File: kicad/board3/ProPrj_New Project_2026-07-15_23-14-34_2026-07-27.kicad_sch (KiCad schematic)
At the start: 143 parts, among them P1 WJ500V-5.08-2P, P2 WJ500V-5.08-2P, Q1 AO4406A, Q2 AO4406A, SW1 HX TS4538CJ 250gf 009, SW2 HX TS4538CJ 250gf 009, SW3 HX TS4538CJ 250gf 009, SW4 HX TS4538CJ 250gf 009, SW6 HX TS4538CJ 250gf 009, SW7 HX TS4538CJ 250gf 009, U1 STM32H755ZIT6, U11 AW9523BTQR, U12 AW9523BTQR, U2 W25Q256JVEIQ, U3 TPS563201DDCR, U4 CH224K, U5 LM74700QDBVRQ1, U6 LM74700QDBVRQ1, U7 FM24CL64B-GTR, U8 TJA1051T/3/1J, U9 TJA1051T/3/1J, X1 25MHz

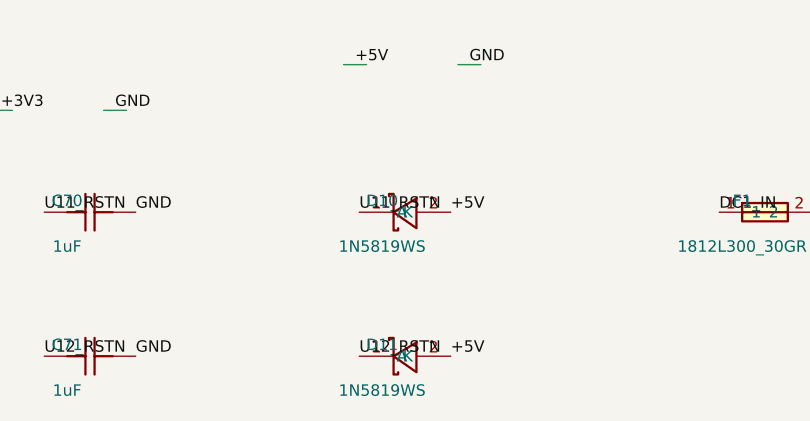
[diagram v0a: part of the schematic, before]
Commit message: fix(kicad): U31 -- reverse D10/D11, the CRITICAL that five of six lenses found
Both Schottkys were installed backwards: cathode on RSTN, anode on +5V, the
opposite of what their own commit message specified. The diode forward-biased
during the rail ramp, so C70/C71 charged through it rather than through R60/R61
and RSTN crossed its fixed 1.4 V VIH at VCC around 1.5-1.6 V -- BELOW VPOR
(1.8 V typ). Reset assertion duration was exactly zero at every ramp rate, and
the brownout half failed in the same direction. Worse than fitting no diode,
which would at least have delivered ~335 us of power-up hold. The 2026-07-31
CRITICAL was never actually closed.

Fixed on both sides with ZERO copper movement.

Schematic: D10/D11 are connected by labels sitting at fixed pin coordinates, not
by drawn wires, so rotating each symbol 180 degrees swaps which pin lands under
which label. The symbol is pin-symmetric (+/-5.08 mm, y=0), so the rotation is
exact.

Board: pads are mirror-exact about the footprint origin -- measured 0 nm error,
+/-1.172 mm, identical sizes -- so a 180 degree rotation puts pad 1 precisely
where pad 2 was. Rotate, then swap the pad nets to match, and every existing
track endpoint still lands on a pad of the correct net. D10 pad 1 now sits at
(95.992, 92.260), exactly where pad 2 was, on the +5V copper.

Doing one half alone is a trap either way: rotating without swapping nets shorts
RSTN to +5V, because pad NUMBERS carry the nets; swapping nets without rotating
leaves the silk cathode band on the wrong end.

VERIFIED BY PIN FUNCTION, not pin number -- KTD27, which is the lesson this
defect taught. The exported netlist now reads:

    /+5V       <- D10 pin 1 func=K_1,  D11 pin 1 func=K_1
    /U11_RSTN  <- D10 pin 2 func=A_2
    /U12_RSTN  <- D11 pin 2 func=A_2

The gate that let this through asserted /U11_RSTN carries IC.23 + R.2 + C.1 +
D.1. Pin 1 IS the cathode, so it passed while the circuit was inverted.

One consequence handled: the rotation carried D10/D11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
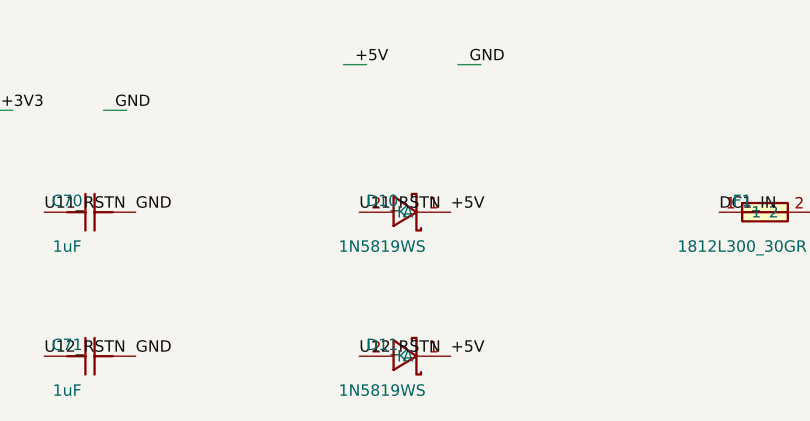
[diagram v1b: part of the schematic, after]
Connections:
- net +5V: now also D10.1 (K), D11.1 (K); no longer D10.2 (A), D11.2 (A)
- net U11_RSTN: now also D10.2 (A); no longer D10.1 (K)
- net U12_RSTN: now also D11.2 (A); no longer D11.1 (K)
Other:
- moved on the sheet: D10, D11
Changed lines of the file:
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@@
 	(symbol
 		(lib_id "JLCImport:1N5819WS")
-		(at 130.0 372.0 0)
+		(at 130.0 372.0 180)
 		(unit 1)
 		(exclude_from_sim no)
@@
 	(symbol
 		(lib_id "JLCImport:1N5819WS")
-		(at 130.0 388.0 0)
+		(at 130.0 388.0 180)
 		(unit 1)
 		(exclude_from_sim no)

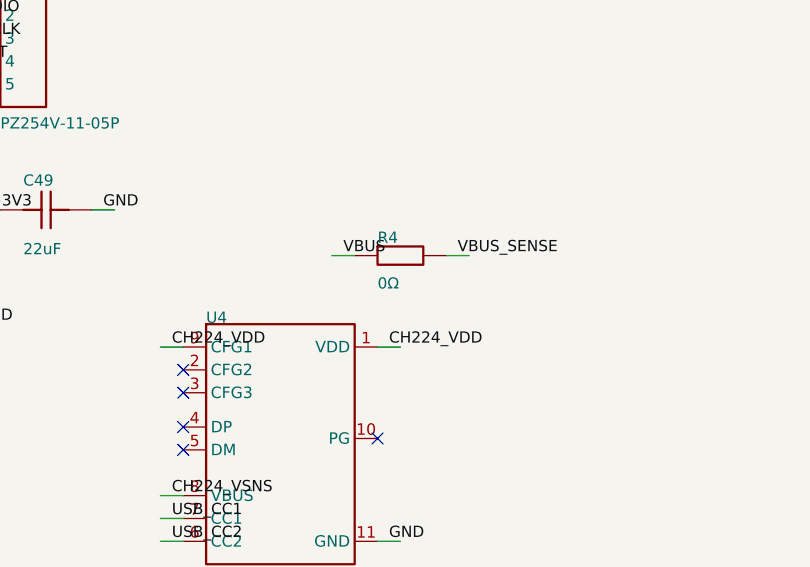
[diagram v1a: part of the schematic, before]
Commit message: fix(kicad): U48 -- R4 0 ohm to 10k, closing the PA9 injection path with no copper
R4 sat at 0 ohm between /VBUS and /VBUS_SENSE, which is a single net reaching
exactly two pads: R4.2 and U1.98 (PA9). PA9 is 5 V tolerant, but ST's tolerance
is conditional on VDD being PRESENT -- and 3.3 V here is DERIVED from 5 V through
U3. So during the buck's soft-start there is a window where 5 V sits on PA9
through 0 ohm while VDD is still rising, and current into the ESD clamp is
limited only by the clamp itself (~10-50 ohm): tens of mA against a documented
+/-5 mA pin injection limit, on EVERY power-up.

The plan called for a 100k/100k divider, which means a new part placed and
routed. 10 kOhm alone does better for zero board change:

  injection during VDD ramp   unlimited  ->  (5 - Vclamp)/10k = ~110 uA
  PA9 with USB absent         floats     ->  pulled low by PA9's internal ~40k
  PA9 with USB present        --         ->  5 x 40/50 = 4.0 V, VIH is 2.31 V

Worst-case internal pull-down across its 30-50k spread gives 3.75-4.17 V, so the
high level holds either way, and the low level no longer depends on nothing.

FIRMWARE DEPENDENCY, and it is load-bearing: PA9 must be configured with its
internal pull-down enabled (GPIOx_PUPDR). Without it the pin still floats when
USB is unplugged and VBUS sensing reads indeterminate -- the hardware half of
this fix is the current limit, the firmware half is the defined low. Nothing
configures PA9 today.

Free consequence: R4 was the board's ONLY 0 ohm part, and 10k on R0603 is
already fitted 12 times. It merges into that line, so the BOM drops 46 -> 45 and
an entire part number leaves the order. Same footprint, so no board edit and no
sync -- the U10/U24 precedent.

DRC unchanged, BOM/CPL symmetric at 143, kicad_lcsc.py check PASS.

Co-Authored-By: Claude Opus 5 (1M context) <noreply@anthropic.com>
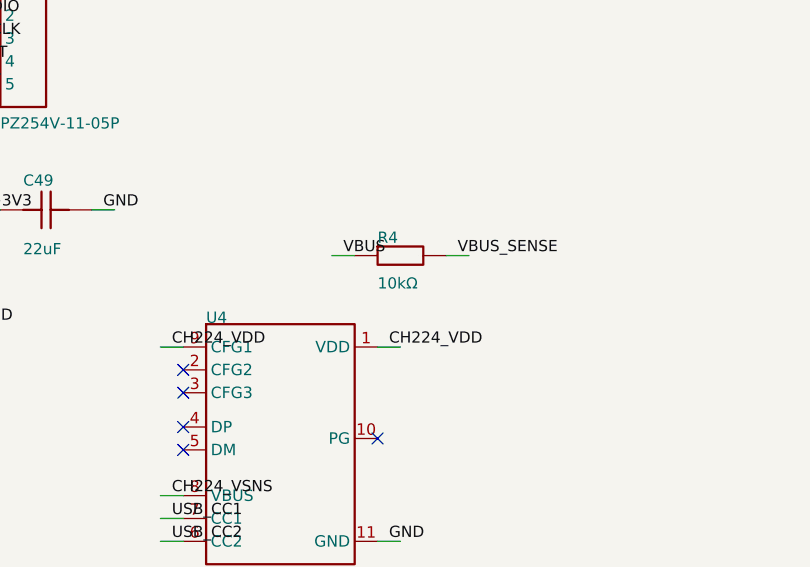
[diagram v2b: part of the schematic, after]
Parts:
- R4: value 0Ω -> 10kΩ; symbol ProPrj_New-easyedapro:0603WAF0000T5E -> ProPrj_New-easyedapro:0603WAF1002T5E; LCSC Part Name 0Ω ±1% 100mW 厚膜电阻 -> 厚膜电阻 10kΩ ±1% 100mW; Manufacturer Part 0603WAF0000T5E -> 0603WAF1002T5E; Supplier Part C21189 -> C25804
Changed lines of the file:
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@@
 	)
 	(symbol
-		(lib_id "ProPrj_New-easyedapro:0603WAF0000T5E")
+		(lib_id "ProPrj_New-easyedapro:0603WAF1002T5E")
 		(at 358.14 59.69 0)
 		(unit 1)
@@
 			)
 		)
-		(property "Value" "0Ω"
+		(property "Value" "10kΩ"
 			(at 355.6 63.5 0)
 			(show_name no)
@@
 			)
 		)
-		(property "Datasheet" "https://item.szlcsc.com/datasheet/0603WAF0000T5E/21903.html"
+		(property "Datasheet" "https://item.szlcsc.com/datasheet/0603WAF1002T5E/26547.html"
 			(at 358.14 59.69 0)
 			(hide yes)
@@
 			)
 		)
-		(property "Description" "Type:Thick Film Resistor Resistance:0Ω Tolerance:±1% Tolerance:±1% Power(Watts):100mW Voltage-Supply(Max):75V Temperature Coefficient:- Temperature Coefficient:- Operating Temperature:-55℃~+155℃ Operating Temperature:-55℃~+155℃"
+		(property "Description" "Type:Thick Film Resistor Resistance:10kΩ Tolerance:±1% Tolerance:±1% Power(Watts):100mW Voltage-Supply(Max):75V Temperature Coefficient:±100ppm/℃ Temperature Coefficient:±100ppm/℃ Operating Temperature:-55℃~+155℃ Operating Temperature:-55℃~+155℃"
 			(at 358.14 59.69 0)
 			(hide yes)
@@
 			)
 		)
-		(property "Manufacturer Part" "0603WAF0000T5E"
+		(property "Manufacturer Part" "0603WAF1002T5E"
 			(at 358.14 59.69 0)
 			(hide yes)
@@
 			)
 		)
-		(property "Supplier Part" "C21189"
+		(property "Supplier Part" "C25804"
 			(at 358.14 59.69 0)
 			(hide yes)
@@
 			)
 		)
-		(property "LCSC Part Name" "0Ω ±1% 100mW 厚膜电阻"
+		(property "LCSC Part Name" "厚膜电阻 10kΩ ±1% 100mW"
 			(at 358.14 59.69 0)
 			(hide yes)

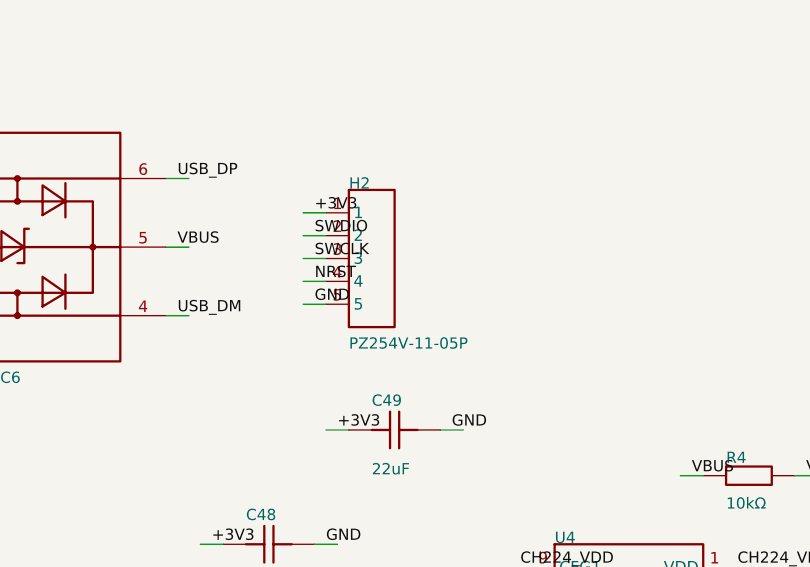
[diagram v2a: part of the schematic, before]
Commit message: feat(kicad): U49 -- H2 Tag-Connect debug header, board side closed
14 DRC errors and the last airwire, to zero. Only the two known
silk_over_copper warnings (U3/U4 circles) remain, unchanged.

H2 is the legless TC2030-IDC-NL: pogo pins press on bare copper, nothing is
fitted. The legged variant was measured and has ZERO feasible placements
within +/-9 mm -- its four 2.37 mm leg holes hit the /NRST bottom run at
every orientation. Footprint lives in a new Board3.pretty, for land patterns
with no purchasable part behind them.

Four fixes, all applied through tools/kicad_handroute.py so the copper is
reviewable as coordinates. The per-segment clearance arithmetic is in the
spec's $why blocks; the reasoning that is expensive to rediscover:

* hole_clearance x12. The four pours fill to min_clearance 0.1016 and so
  land 0.1021 from H2's three 0.9906 NPTH alignment holes, under the 0.2
  min_hole_clearance rule -- 3 holes x 4 zones, with nothing upstream wrong
  to fix. Three footprint-parented octagon keepouts ban only the pour
  (circumradius 0.85 -> inradius 0.7853, so copper stops 0.290 from the hole
  edge, 1.45x the rule). Vias stay LEGAL by design: SWO's own escape via
  lands at (135.212,120.200), inside H2's courtyard, so banning them here
  would have blocked the fourth fix from the other side.

* shorting_items /BTN2 <-> /NRST. The bottom straight at x=133.500 ran 0.100
  from the /BTN2 via at (133.400,115.200), against the 0.5286 a 0.6 via
  needs. A via is a disc on EVERY layer, so checking that segment against
  Bottom copper alone finds nothing -- the full-layer sweep also turned up
  /BTN1 at (136.000,113.600). The jog clears both, by 0.700 and 1.923.

* hole_clearance on /+3V3. The pad-1 escape passed 0.162 from the hole at
  (131.402,121.588) -- through it. That via sits only 1.330 from the hole, so
  the tangents to the 0.8223 keep-out circle are 38.2 deg either side and
  EVERY approach between 5.6 and 82.0 deg clips it. Hence an L approaching
  due so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
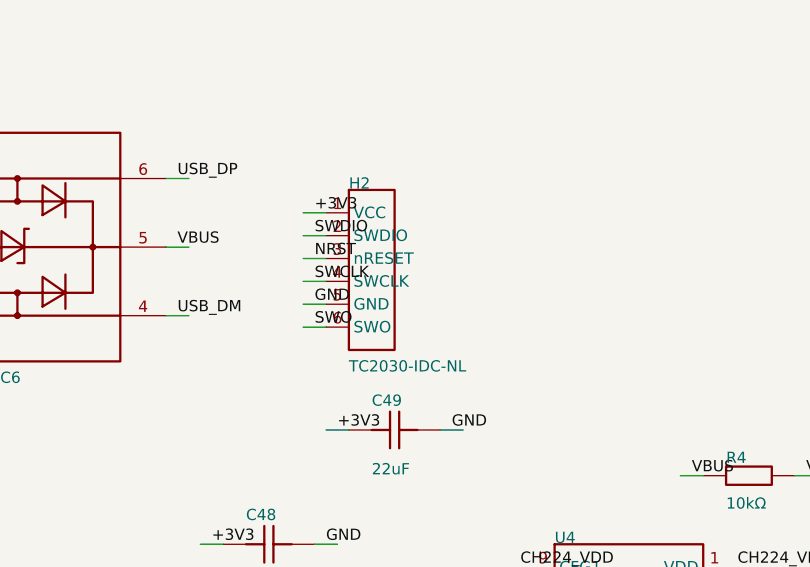
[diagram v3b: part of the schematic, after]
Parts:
- H2: value PZ254V-11-05P -> TC2030-IDC-NL; footprint ProPrj_New-easyedapro:HDR-TH_5P-P2.54-V-M -> Board3:Tag-Connect_TC2030-IDC-NL_2x03_P1.27mm_Vertical; symbol ProPrj_New-easyedapro:PZ254V-11-05P -> Board3:TC2030-IDC-NL; Add into BOM yes -> (none); Circluar Pins/Square Pins Pin Header -> (none); Color Black -> (none); Contact Material Brass -> (none); Contact Plating - -> (none); Convert to PCB yes -> (none); Current Rating 3A -> (none); Insulation Height 2.5mm -> (none); JLCPCB Part Class Extended Part -> (none); LCSC Part Name 1x5P 间距:2.54mm 方针 直插 -> (none); Length of End Connection Pin 3mm -> (none); Length of Mating Pin 6mm -> (none); Manufacturer XFCN(兴飞) -> (none); Manufacturer Part PZ254V-11-05P -> (none); Mounting Type Through Hole -> (none); Number of Pins 5P -> (none); Number of Rows 1 -> (none); Operating Temperature -40℃~+105℃ -> (none); Pin Structure 1x5P -> (none); Pitch 2.54mm -> (none); Row Spacing - -> (none); Supplier LCSC -> (none); Supplier Footprint 插件,P=2.54mm -> (none); Supplier Part C492404 -> (none); Voltage Rating (Max) 250V -> (none); now left out of the parts list
- L1: LCSC Part Name 单路 0603磁珠 阻抗120Ω@100MHz -> 单路 0603磁珠 阻抗120Ω100MHz
- Q1, Q2: Gate Charge(Qg) 12.6nC@4.5V -> 12.6nC4.5V; Gate Threshold Voltage (Vgs(th)) 1.5V@250uA -> 1.5V250uA; RDS(on) 10mΩ@10V -> 10mΩ10V; Reverse Transfer Capacitance (Crss@Vds) 87pF -> (none); Reverse Transfer Capacitance (CrssVds) (none) -> 87pF
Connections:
- net NRST: now also H2.3 (nRESET); no longer H2.4
- net SWCLK: now also H2.4 (SWCLK); no longer H2.3
- net SWO: now also H2.6 (SWO)

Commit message: fix(kicad): U36 -- C67 to 22 uF/0805, BOM 44 lines to 43
C67 was the odd one out of the three panel bulk caps: C66 at FPC1 and C68 at
FPC3 are 22 uF/0805, C67 at FPC2 was 10 uF/0603. That 0603 land was inherited
from the EasyEDA import rather than chosen, and C67 was the board's only 10 V
part -- the most heavily DC-bias-derated component here, delivering nearer
5 uF at 3.3 V against its siblings' ~17 uF. FPC2 now matches its neighbours.

It also deletes a workaround at the root. C67 and C51 were both 10uF in
different packages, which collided in the JLCPCB uploader's Comment column and
made kicad_fab.py disambiguate them on every run. That code path no longer
fires: C67 joins C29/C30/C31/C48/C49/C66/C68 as the eighth C45783.

Schematic and board were edited independently and the new --schematic-parity
gate proves they agree -- which is what made this safe to do without the GUI
sync. Value, Footprint, Datasheet, Manufacturer Part and Supplier Part moved
together; the .kicad_sch was patched by line anchor with its CRLF preserved.

The copper took three findings to land:

* The /+3V3 side needed nothing. Its track started at (140.350,92.000), which
  the larger pad 1 still covers.
* The /GND stitching via at (140.350,94.300) ended up INSIDE the new pad 2.
  Same net, so DRC would never have said a word -- it would simply have been a
  via in a pad, wicking solder down the barrel at reflow. Moved east to
  (141.000,94.900): it cannot go south, because the /I2C_SCL Inner1 diagonal
  overhead caps it at y <= 94.702 while clearing the pad needs y > 94.705.
* The 0805 pad then starved C47 pad 2's thermal relief -- 1 spoke against the
  required 2. Not the west gap: that was already 1.0 mm. C67 moves 0.5 mm west
  in total, chosen by bisection, because the clean window is narrow. At -0.3 mm
  the thermal starves, at -0.7 mm the courtyards overlap, and past -0.9 mm the
  /+3V3 track stops landing on the pad. -0.5 sits mid-window, 0.1 mm either side.

One methodology note wor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
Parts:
- C67: value 10uF -> 22uF; footprint ProPrj_New-easyedapro:C0603 -> ProPrj_New-easyedapro:C0805; Manufacturer Part CL10A106KP8NNNC -> CL21A226MAQNNNE; Supplier Part C19702 -> C45783
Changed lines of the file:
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@@
 			)
 		)
-		(property "Value" "10uF"
+		(property "Value" "22uF"
 			(at 129.54 292.1 0)
 			(show_name no)
@@
 			)
 		)
-		(property "Footprint" "ProPrj_New-easyedapro:C0603"
+		(property "Footprint" "ProPrj_New-easyedapro:C0805"
 			(at 132.08 287.02 0)
 			(hide yes)
@@
 			)
 		)
-		(property "Datasheet" "https://item.szlcsc.com/datasheet/CL10A106KP8NNNC/19702.html"
+		(property "Datasheet" "https://item.szlcsc.com/datasheet/CL21A226MAQNNNE/45783.html"
 			(at 132.08 287.02 0)
 			(hide yes)
@@
 			)
 		)
-		(property "Manufacturer Part" "CL10A106KP8NNNC"
+		(property "Manufacturer Part" "CL21A226MAQNNNE"
 			(at 132.08 287.02 0)
 			(hide yes)
@@
 			)
 		)
-		(property "Supplier Part" "C19702"
+		(property "Supplier Part" "C45783"
 			(at 132.08 287.02 0)
 			(hide yes)

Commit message: fix(kicad): U42 -- delete the mid-point caps; CAN termination is balanced again
The defect U42 exists to fix: H1 and H3 sit only in the CAN_H branch, so with a
jumper OPEN the CAN_L line still carried 60.4 ohm + 4.7 nF to ground,
permanently. That is an unbalanced AC load on one leg of a differential pair --
tau = 284 ns against a 1 us bit time at 1 Mbps -- and it is exactly what split
termination exists to avoid. kicad_rules.json records the intended default as
un-terminated, so the un-jumpered state was the one that was wrong.

The fix is smaller than the plan assumed, because R10/R14 and R15/R24 are
ALREADY in series: 60.4 + 60.4 = 120.8 ohm between CAN_TERM and CAN_L. The only
thing making that a SPLIT termination is the mid-point cap tapping to ground.
Delete C57 and C58 and the network becomes exactly what U42 asked for:

  jumper fitted -> 120.8 ohm across the pair, standard end termination
  jumper open   -> the resistors dangle from CAN_L with their far end floating,
                   no path to ground at all

120.8 ohm is inside a 120 ohm +/-1% window (118.8-121.2), so this is the target
value, not an approximation of it.

Verified on the NETLIST rather than by inspection, because the risk here was a
short: deleting a symbol can leave two wire stubs that merge the nets it used to
separate. /CAN1_CT is {R10.2, R14.1} and /CAN2_CT is {R15.2, R24.1} -- plain
series junctions with no capacitor and no ground -- /GND carries no C57/C58, and
228 nets parse. No short.

What is NOT done, deliberately: the plan also wanted 2 x 60.4 ohm consolidated
into 1 x 120 ohm (C22787, Basic + preferred) per bus, which would drop two
placements and an extended-part fee. That is a cost optimisation, not the
defect, and it needs a schematic rewire plus copper across both CAN areas. The
defect is closed without it.

One trap worth recording: the first board-side delete matched only 3 of 7
targets because I keyed the coordinates off a 3-decimal dump -- the stored
values are 163446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
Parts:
- removed C57, C58: 4.7nF, ProPrj_New-easyedapro:C0603, symbol ProPrj_New-easyedapro:0603B472K500NT
